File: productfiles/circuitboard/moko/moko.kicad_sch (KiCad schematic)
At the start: 39 parts, among them J1 Conn_01x06, J2 AudioJack4, J3 Conn_01x06, SW1 SW_PUSH, SW10 SW_PUSH, SW11 SW_PUSH, SW12 SW_PUSH, SW13 SW_PUSH, SW14 SW_PUSH, SW15 SW_PUSH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

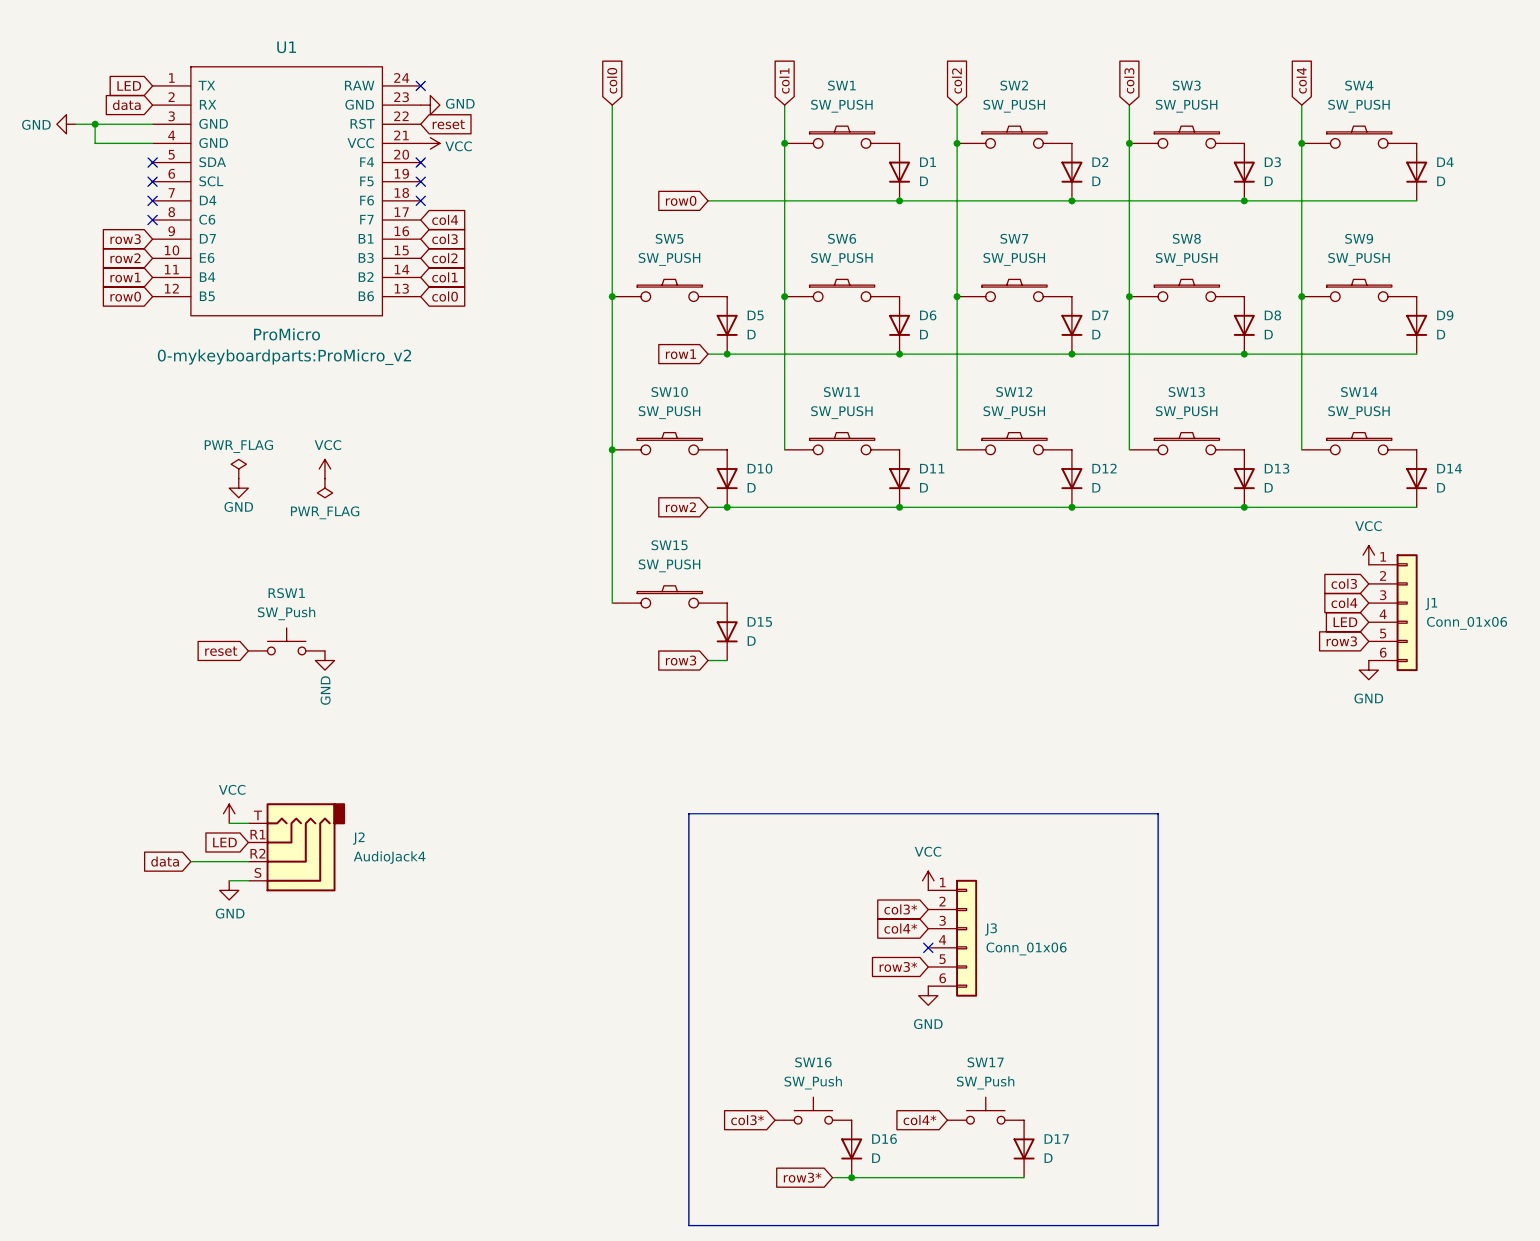
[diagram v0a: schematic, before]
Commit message: add choc layout
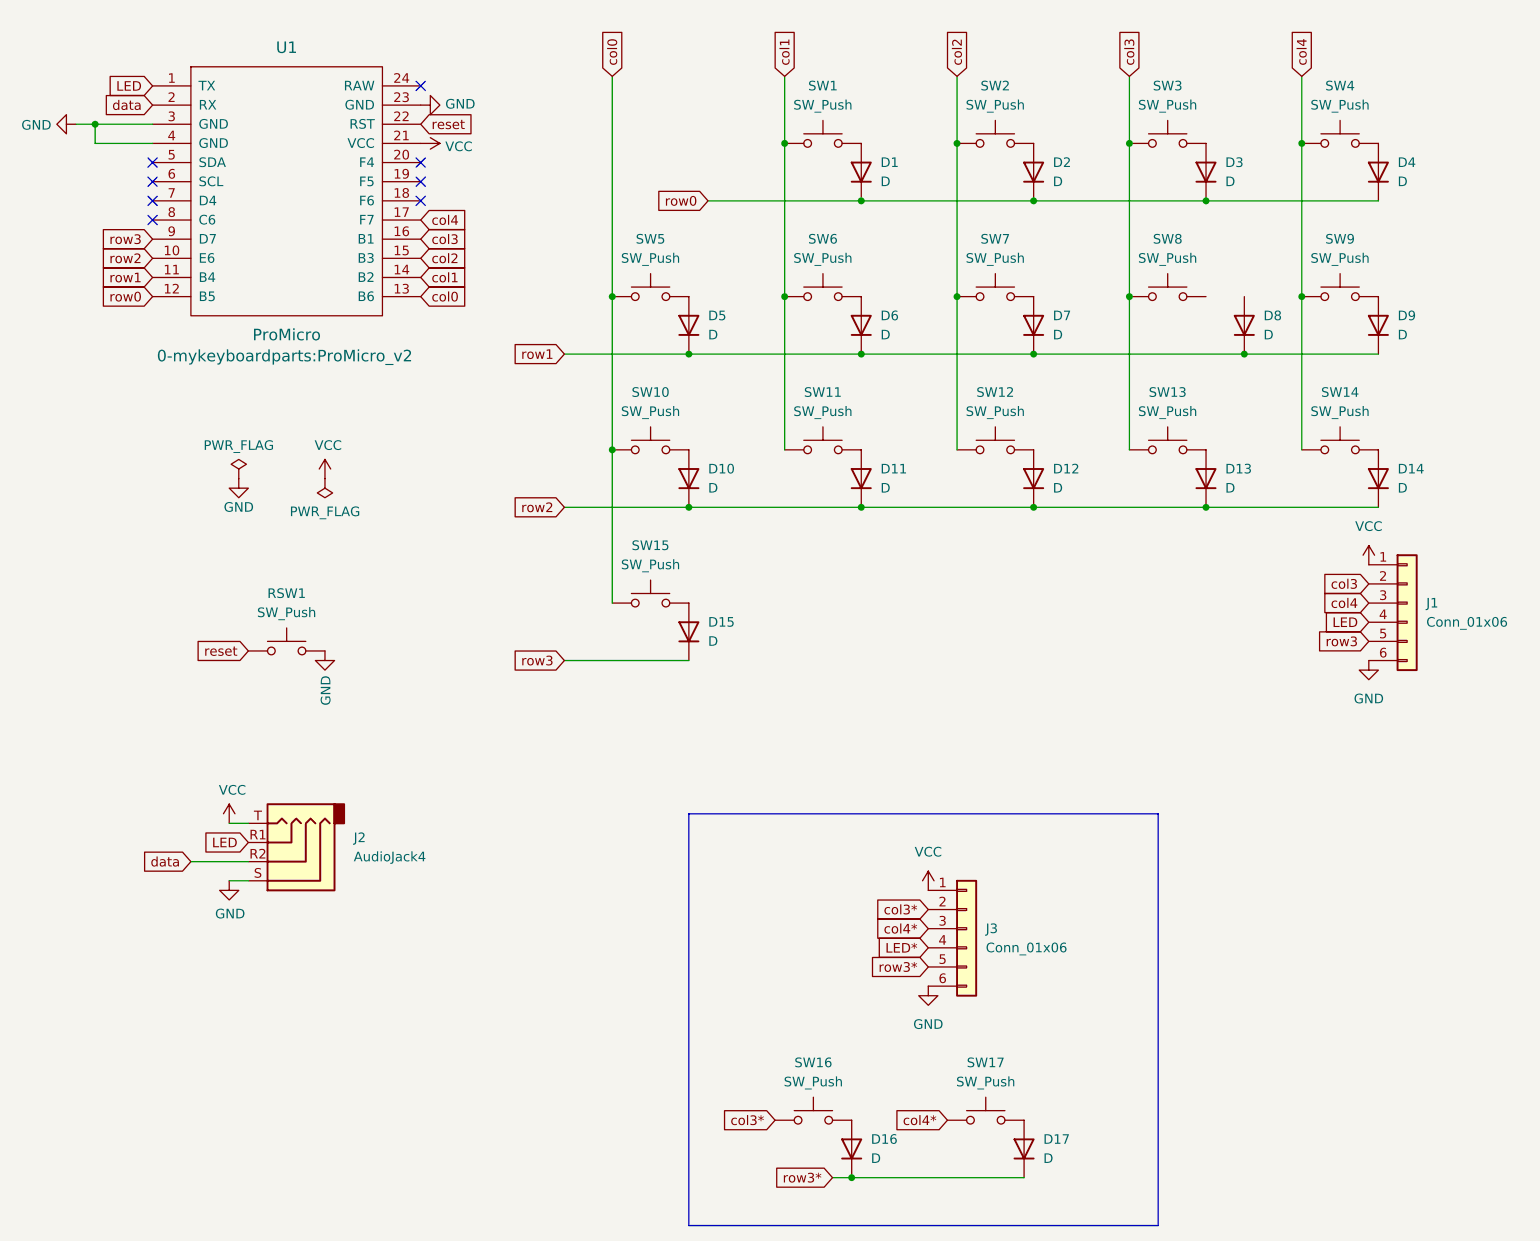
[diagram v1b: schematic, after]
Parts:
- SW1, SW10, SW11, SW12, SW13, SW14, SW15, SW2, SW3, SW4, SW5, SW6, SW7, SW8, SW9: value SW_PUSH -> SW_Push; footprint (none) -> 0-keebparts:CherryMX_Choc_Hotswap; symbol 0-kbd:SW_PUSH -> Switch:SW_Push
- SW16, SW17: footprint (none) -> 0-keebparts:CherryMX_Choc_Hotswap
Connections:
- net at SW8.2: no longer D8.2 (A)
- net LED*: now reaches J3.4 (Pin_4)
- no-connect marks 9 -> 8
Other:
- moved on the sheet: D1, D10, D11, D12, D13, D14, D15, D2, D3, D4, D5, D6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
